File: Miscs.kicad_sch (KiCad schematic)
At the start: 14 parts, among them U7 THGBMUG6C1LBAIL

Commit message: Chore: push new design
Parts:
- removed BZ1: PKMCS0909E4000-R1, Buzzer_Beeper:PUIAudio_SMT_0825_S_4_R, symbol Device:Buzzer
- removed R8: 470Ω, PCM_JLCPCB:R_0603, symbol PCM_JLCPCB-Resistors:0402,470Ω
- added LS1: PS1440P02BT, Snapeda:PS1440P02BT_BUZZER_PS1440P02BT, symbol Snapeda:PS1440P02BT
- added R5: 1kΩ, PCM_JLCPCB:R_0603, symbol PCM_JLCPCB-Resistors:0603,1kΩ
- C73: footprint PCM_JLCPCB:C_0402 -> PCM_JLCPCB:C_0603
- R49, R50, R51, R52, R53, R54, R55, R56, R57, R58: footprint PCM_JLCPCB:R_0402 -> PCM_JLCPCB:R_0603
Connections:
- net BUZZER: now also LS1.1
- net GND: now also R5.2
- new net: LS1.2, R5.1

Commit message: Special version
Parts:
- C73: Digikey Parts (none) -> CL10A106KP8NNNC
- R49, R50, R51, R52, R53, R54, R55, R56, R57: Digikey Parts (none) -> RC0603FR-0722KL
- R5: Digikey Parts (none) -> RC0603JR-071KL
- R58: Digikey Parts (none) -> RC0603FR-0747KL
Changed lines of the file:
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@@
 			)
 		)
+		(property "Digikey Parts" "RC0603FR-0722KL"
+			(at 72.39 78.74 0)
+			(effects
+				(font
+					(size 1.27 1.27)
+				)
+			)
+		)
 		(pin "1"
 		)
@@
 			)
 		)
+		(property "Digikey Parts" "CL10A106KP8NNNC"
+			(at 53.34 137.16 0)
+			(effects
+				(font
+					(size 1.27 1.27)
+				)
+			)
+		)
 		(pin "2"
 		)
@@
 			)
 		)
+		(property "Digikey Parts" ""
+			(at 193.04 39.37 0)
+			(effects
+				(font
+					(size 1.27 1.27)
+				)
+			)
+		)
 		(pin "1"
 		)
@@
 			)
 		)
+		(property "Digikey Parts" "RC0603FR-0722KL"
+			(at 67.31 43.18 0)
+			(effects
+				(font
+					(size 1.27 1.27)
+				)
+			)
+		)
 		(pin "1"
 		)
@@
 			)
 		)
+		(property "Digikey Parts" "RC0603FR-0722KL"
+			(at 67.31 78.74 0)
+			(effects
+				(font
+					(size 1.27 1.27)
+				)
+			)
+		)
 		(pin "1"
 		)
@@
 			)
 		)
+		(property "Digikey Parts" "RC0603FR-0722KL"
+			(at 50.8 78.74 0)
+			(effects
+				(font
+					(size 1.27 1.27)
+				)
+			)
+		)
 		(pin "1"
 		)
@@
 			)
 		)
+		(property "Digikey Parts" "RC0603FR-0722KL"
+			(at 62.23 43.18 0)
+			(effects
+				(font
+					(size 1.27 1.27)
+				)
+			)
+		)
 		(pin "1"
 		)
@@
 			)
 		)
+		(property "Digikey Parts" ""
+			(at 90.17 143.51 0)
+			(effects
+				(font
+					(size 1.27 1.27)
+				)
+			)
+		)
 		(pin "A13"
 		)
@@
 			)
 		)
+		(property "Digikey Parts" "RC0603FR-0722KL"
+			(at 72.39 43.18 0)
+			(effects
+				(font
+					(size 1.27 1.27)
+				)
+			)
+		)
 		(pin "1"
 		)
@@
 			)
 		)
+		(property "Digikey Parts" "RC0603JR-071KL"
+			(at 198.12 45.72 0)
+			(effects
+				(font
+					(size 1.27 1.27)
+				)
+			)
+		)
 		(pin "1"
 		)
@@
 			)
 		)
+		(property "Digikey Parts" "RC0603FR-0722KL"
+			(at 55.88 78.74 0)
+			(effects
+				(font
+					(size 1.27 1.27)
+				)
+			)
+		)
 		(pin "1"
 		)
@@
 			)
 		)
+		(property "Digikey Parts" "RC0603FR-0747KL"
+			(at 140.97 135.89 0)
+			(effects
+				(font
+					(size 1.27 1.27)
+				)
+			)
+		)
 		(pin "2"
 		)
@@
 			)
 		)
+		(property "Digikey Parts" "RC0603FR-0722KL"
+			(at 62.23 78.74 0)
+			(effects
+				(font
+					(size 1.27 1.27)
+				)
+			)
+		)
 		(pin "1"
 		)
@@
 			(at 106.68 236.22 0)
 			(effects
+				(font
+					(size 1.27 1.27)
+				)
+			)
+		)
+		(property "Digikey Parts" "RC0603FR-0722KL"
+			(at 106.68 236.22 0)
+			(effects

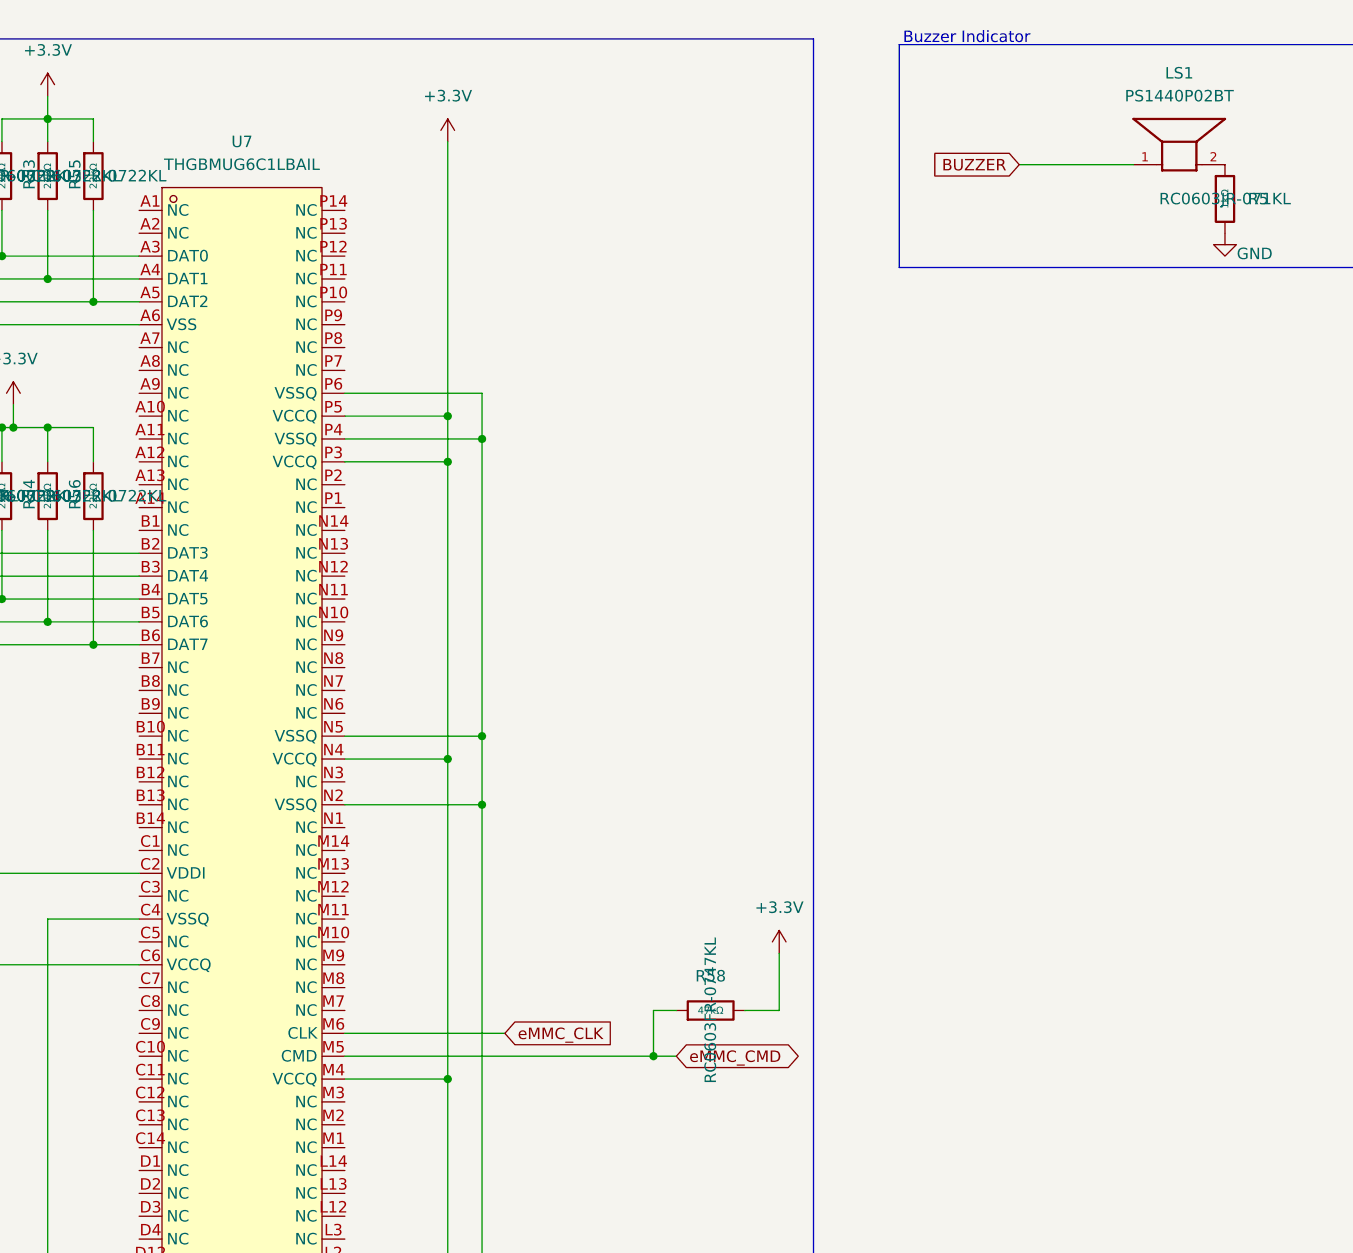
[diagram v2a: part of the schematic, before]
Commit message: Chore: Add Digikey Part to symbols
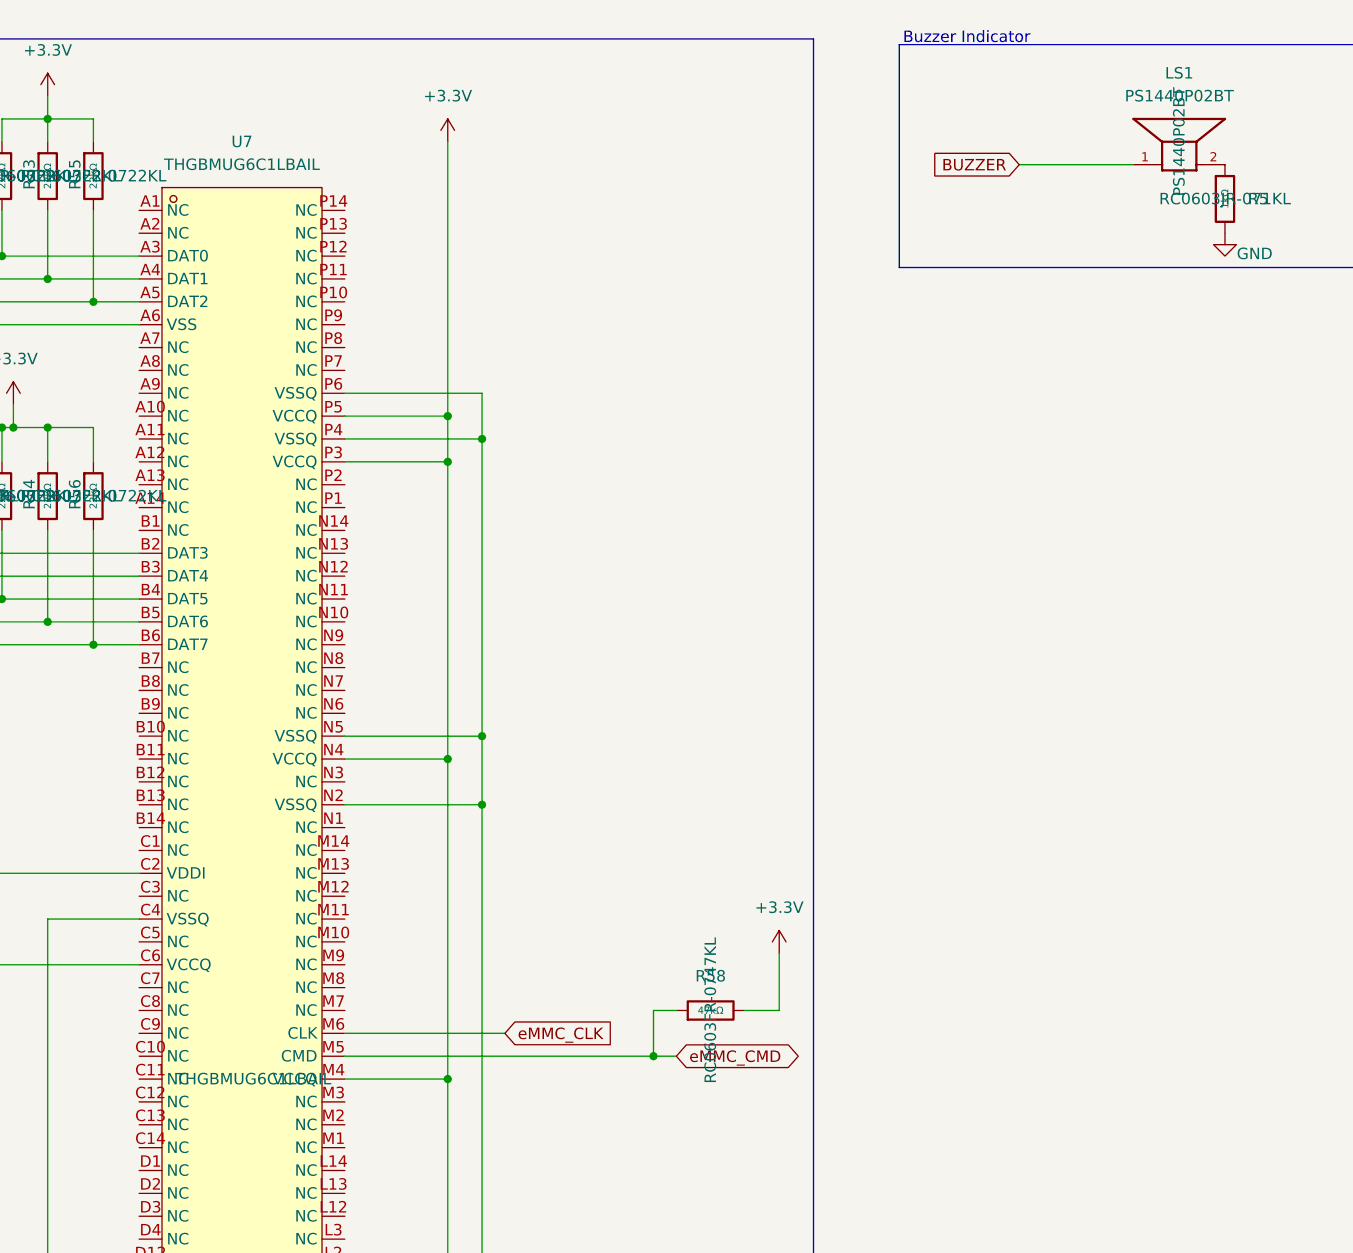
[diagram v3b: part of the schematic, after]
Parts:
- LS1: Digikey Parts (none) -> PS1440P02BT
- U7: Digikey Parts (none) -> THGBMUG6C1LBAIL
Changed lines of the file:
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@@
 			)
 		)
-		(property "Digikey Parts" ""
+		(property "Digikey Parts" "PS1440P02BT"
 			(at 193.04 39.37 0)
 			(effects
@@
 			)
 		)
-		(property "Digikey Parts" ""
+		(property "Digikey Parts" "THGBMUG6C1LBAIL"
 			(at 90.17 143.51 0)
 			(effects

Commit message: Complete Redesign
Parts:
- added J8: MEM2080-00-128-00-A_REVA, SDCard:GCT_MEM2080-00-128-00-A_REVA, symbol MEM2080-00-128-00-A_REVA:MEM2080-00-128-00-A_REVA
- added R23, R25, R26, R27, R28, R29, R30, R32, R33, R35: 10kΩ, PCM_JLCPCB:R_0603, symbol PCM_JLCPCB-Resistors:0603,10kΩ
- added R31: 1MΩ, PCM_JLCPCB:R_0603, symbol PCM_JLCPCB-Resistors:0603,1MΩ
- added U11: XTSD08GLGEAG, EasyEDA:LGA-8_L6.0-W8.0-P1.27-BL, symbol EasyEDA:XTSD08GLGEAG
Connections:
- net +3.3V: now also R23.1, R25.1, R26.1, R27.1, R28.1, R29.1, R30.1, R32.1, R33.1, R35.1, U11.8 (Vdd)
- net DAT0: now also J8.P7 (DAT0), R23.2, R30.2, U11.6 (SD0/DO)
- net DAT1: now also J8.P8 (DAT1), R25.2, R29.2, U11.7 (SD1/NC)
- net DAT2: now also J8.P1 (DAT2), R26.2, R28.2, U11.1 (SD2/NC)
- net DAT3: now also J8.P2 (CD/DAT3), R32.2, R35.2, U11.2 (SD3/~{CS})
- net GND: now also J8.P6 (VSS), R31.2, U11.4 (Vss)
- net eMMC_CLK: now also J8.P5 (CLK), U11.3 (CLK)
- net eMMC_CMD: now also J8.P3 (CMD), R27.2, R33.2, U11.5 (CMD/DI)
- new net: J8.S1 (SHIELD), J8.S2 (SHIELD__1), J8.S3 (SHIELD__2), J8.S4 (SHIELD__3), R31.1
- no-connect marks 0 -> 2

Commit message: 1
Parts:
- removed C73: 10uF, PCM_JLCPCB:C_0603, symbol PCM_JLCPCB-Capacitors:0402,10uF
- removed R49, R50, R51, R52, R53, R54, R55, R56, R57: 22kΩ, PCM_JLCPCB:R_0603, symbol PCM_JLCPCB-Resistors:0402,22kΩ
- removed R58: 47kΩ, PCM_JLCPCB:R_0603, symbol PCM_JLCPCB-Resistors:0402,47kΩ
- removed U7: THGBMUG6C1LBAIL, EasyEDA:BGA-153_L13.0-W11.5-P0.50-TL_KLM8G1GEME-B041, symbol EasyEDA:THGBMUG6C1LBAIL
- added C32: 100nF, PCM_JLCPCB:C_0603, symbol PCM_JLCPCB-Capacitors:0402,100nF
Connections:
- net +3.3V: now also J8.P4 (VDD), C32.1
- net GND: now also C32.2
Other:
- note removed: "eMMC"
- moved on the sheet: J8, LS1, R23, R25, R26, R27, R28, R29, R30, R31, R32, R33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

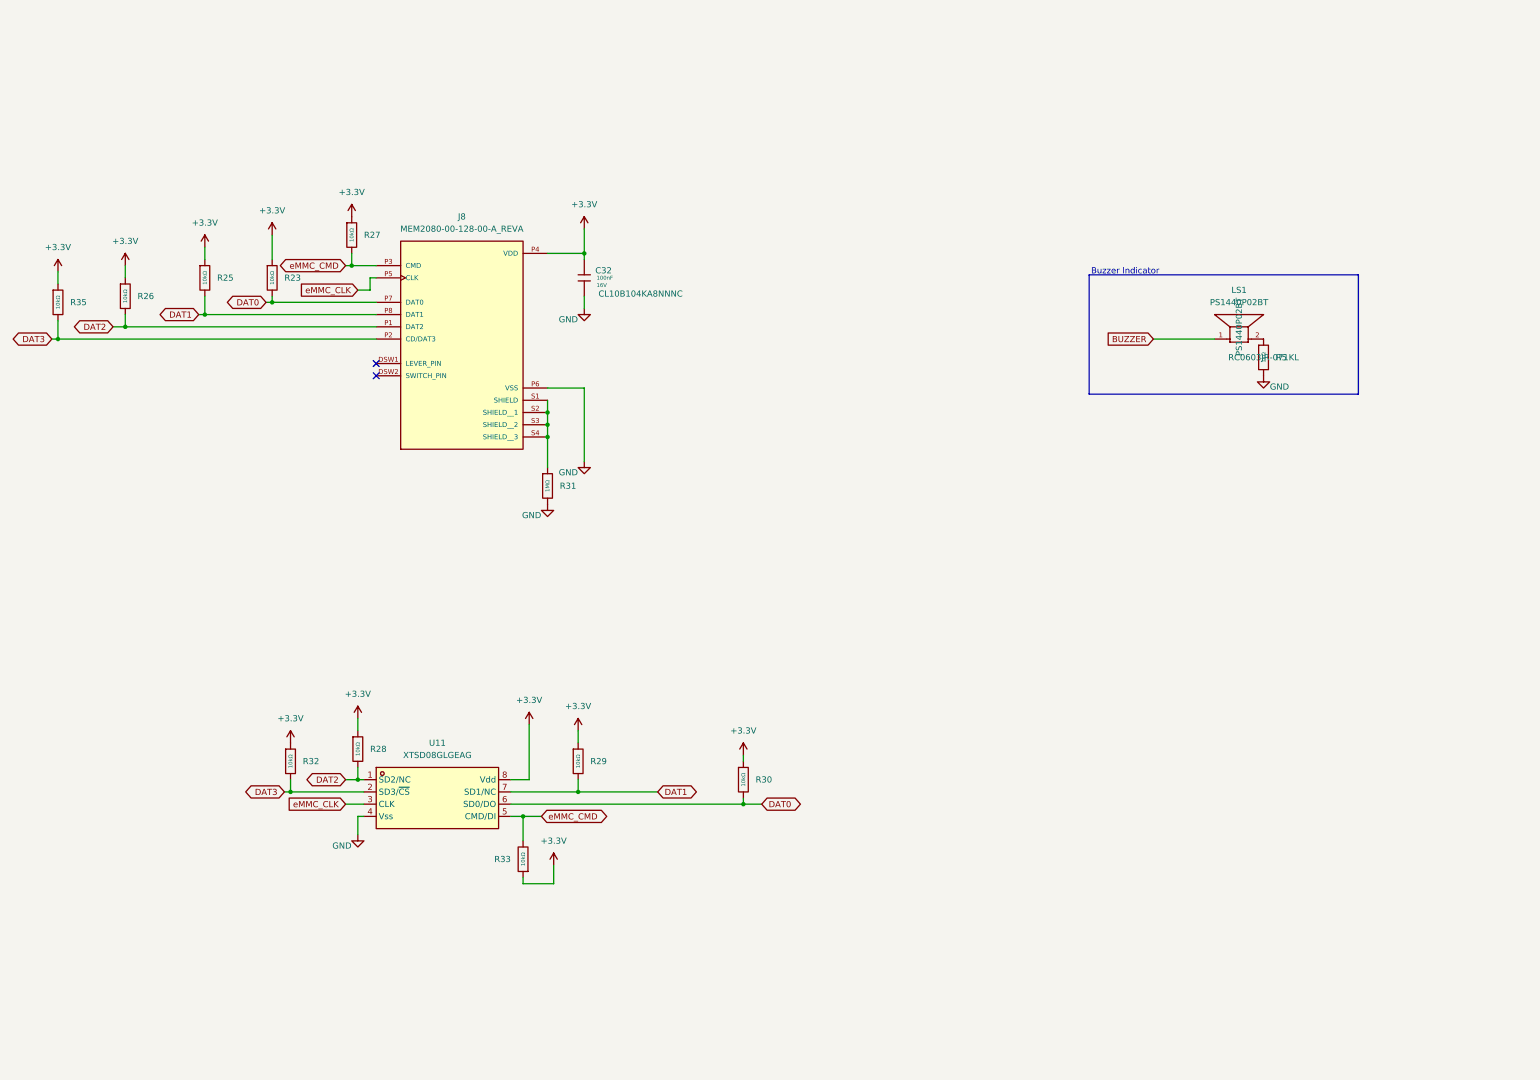
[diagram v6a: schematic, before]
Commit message: Added silkscreen + Changed gps vbackup
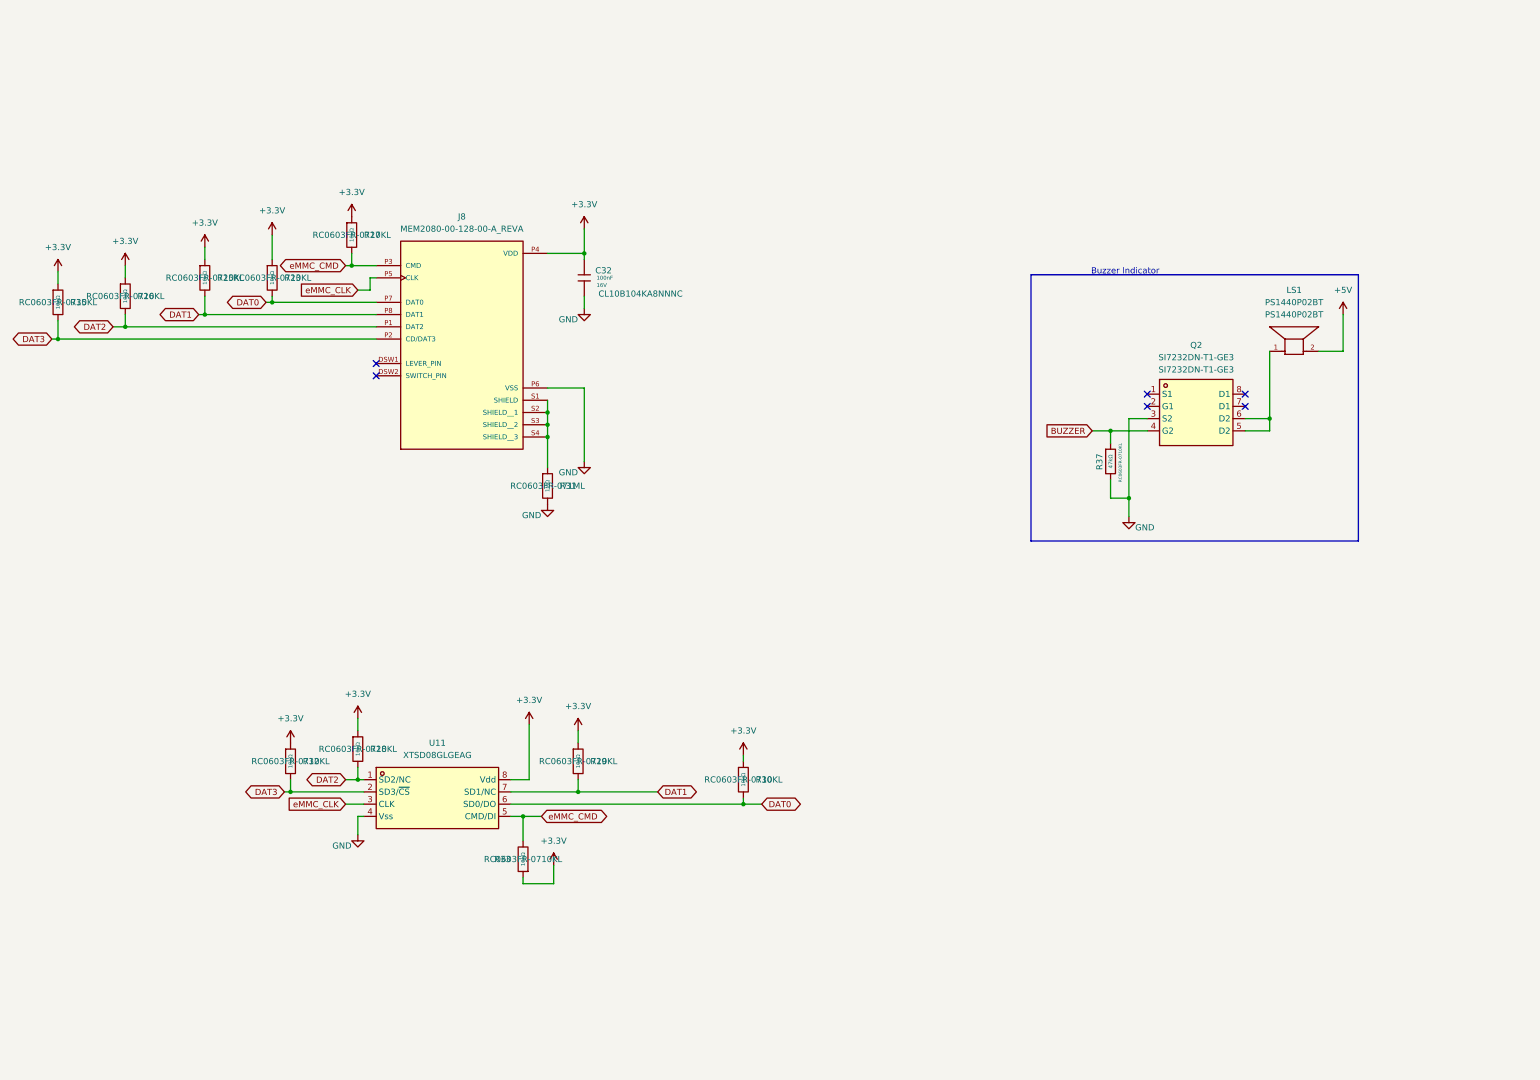
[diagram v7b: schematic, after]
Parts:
- removed R5: 1kΩ, PCM_JLCPCB:R_0603, symbol PCM_JLCPCB-Resistors:0603,1kΩ
- added Q2: SI7232DN-T1-GE3, EasyEDA:POWER-1212-8_L3.3-W3.3-P0.66-LS3.3-BL, symbol EasyEDA:SI7232DN-T1-GE3
- added R37: 47kΩ, PCM_JLCPCB:R_0603, symbol PCM_JLCPCB-Resistors:0402,3.3kΩ
- J8: Digikey Parts (none) -> MEM2080-00-128-00-A
- R23, R25, R26, R27, R28, R29, R30, R32, R33, R35: Digikey Parts (none) -> RC0603FR-0710KL
- R31: Digikey Parts (none) -> RC0603FR-071ML
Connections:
- net BUZZER: now also Q2.4 (G2), R37.1; no longer LS1.1
- net GND: now also Q2.3 (S2), R37.2
- net +5V: now reaches LS1.2
- new net: LS1.1, Q2.5 (D2), Q2.6 (D2)
- no-connect marks 2 -> 6
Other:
- moved on the sheet: LS1

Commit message: adjustments
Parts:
- added C35: 100nF, PCM_JLCPCB:C_0603, symbol PCM_JLCPCB-Capacitors:0402,100nF
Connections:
- net +5V: now also C35.1
- net GND: now also C35.2
